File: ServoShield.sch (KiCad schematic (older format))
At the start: 54 parts, among them P1 M03, P10 M03, P11 M03, P12 M03, P13 M03, P14 M03, P15 M03, P16 M03, P2 M03, P3 M03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

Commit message: Completed v1.0
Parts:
- R9: value 14k -> 8K
- gave numbers to parts that had none: 1
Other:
- note added: "1.5A max output current\n"
- note added: "6V 1.5A Servo Power Supply\n"
- note added: "Default i2c\nAddress 0x40"
- note removed: "1A max output current\n"
- note removed: "6V 1A Servo Power Supply\n"

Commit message: Small tweaks
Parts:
- C1, C5: value 10uF -> 10uF 10V
- C2: value 68uF 25V -> 68uF 10V
- C3, C7: value 1uF -> 1uF 25V
- D1: value B540C -> B340 40V 3A

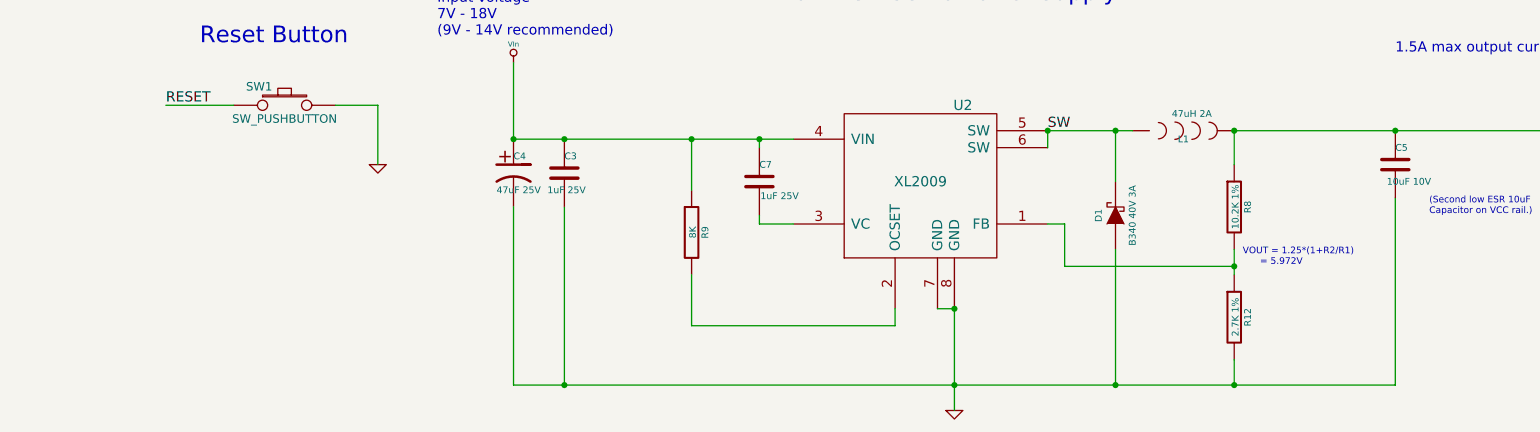
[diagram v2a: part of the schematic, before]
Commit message: V1.1: Add power LED, fix SSOP footprint for PCA9685
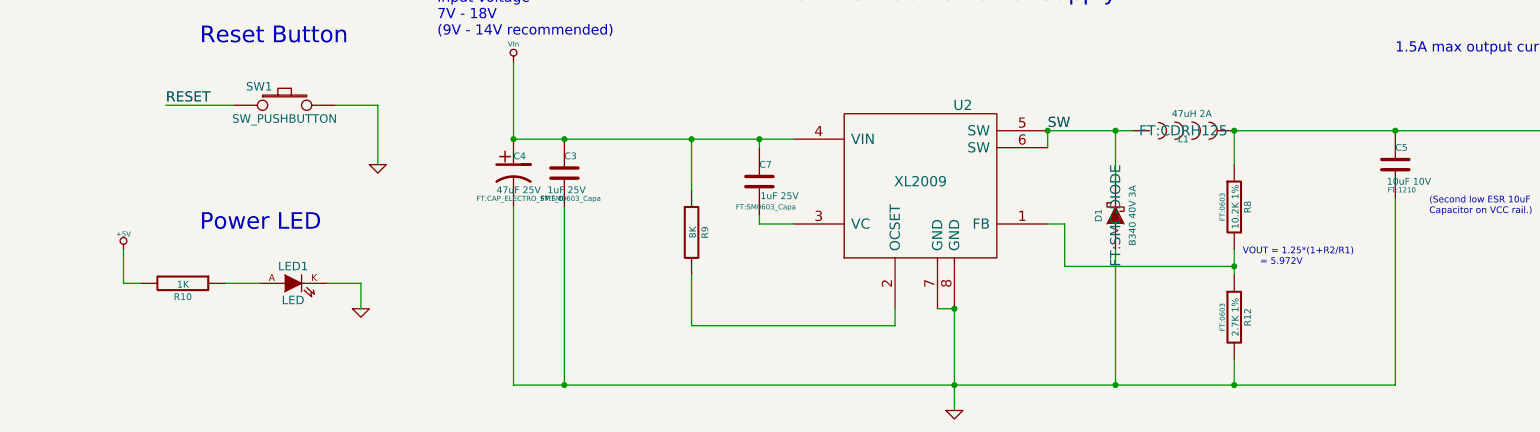
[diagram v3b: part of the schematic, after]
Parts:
- added LED1: LED, FT:LED-0603, symbol LED
- added R10: 1K, FT:0603, symbol R
- C1: footprint (none) -> FT:1210
- C2: footprint (none) -> FT:CAP_ELECTRO_SMT_D
- C3, C7: footprint ~ -> FT:SM0603_Capa
- C4: footprint ~ -> FT:CAP_ELECTRO_SMT_D
- C5: footprint ~ -> FT:1210
- C6: footprint (none) -> FT:SM0603_Capa
- D1: footprint ~ -> FT:SMC-DIODE
- JP1, JP4: footprint (none) -> FT:1X08
- JP2: footprint (none) -> FT:1X06
- JP3: footprint (none) -> FT:1X10
- JP5, P1, P10, P11, P12, P13, P14, P15, P16, P2, P3, P4, P5, P6, P7, P8, P9: footprint (none) -> FT:1X03
- L1: footprint ~ -> FT:CDRH125
- Q1, Q2: footprint (none) -> FT:SOT323_MOSFET
- R1, R2, R3, R4, R6, R7: footprint (none) -> FT:RES_CAY16
- R12, R8: footprint ~ -> FT:0603
- R5, R9: footprint (none) -> FT:0603
- SHIELD1: footprint (none) -> FT:ARDUINO_SHIELD
- SJ1, SJ2, SJ3, SJ4, SJ5, SJ6, SJ7, SJ8: footprint (none) -> FT:SJ_OPEN
- SW1: footprint (none) -> FT:TACTILE_SWITCH_SMD_2PIN_TINY
- U1: footprint (none) -> FT:SSOP28-4.4MM
- U2: footprint (none) -> FT:SO08
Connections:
- wire segments 255 -> 260
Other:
- note added: "Power LED"

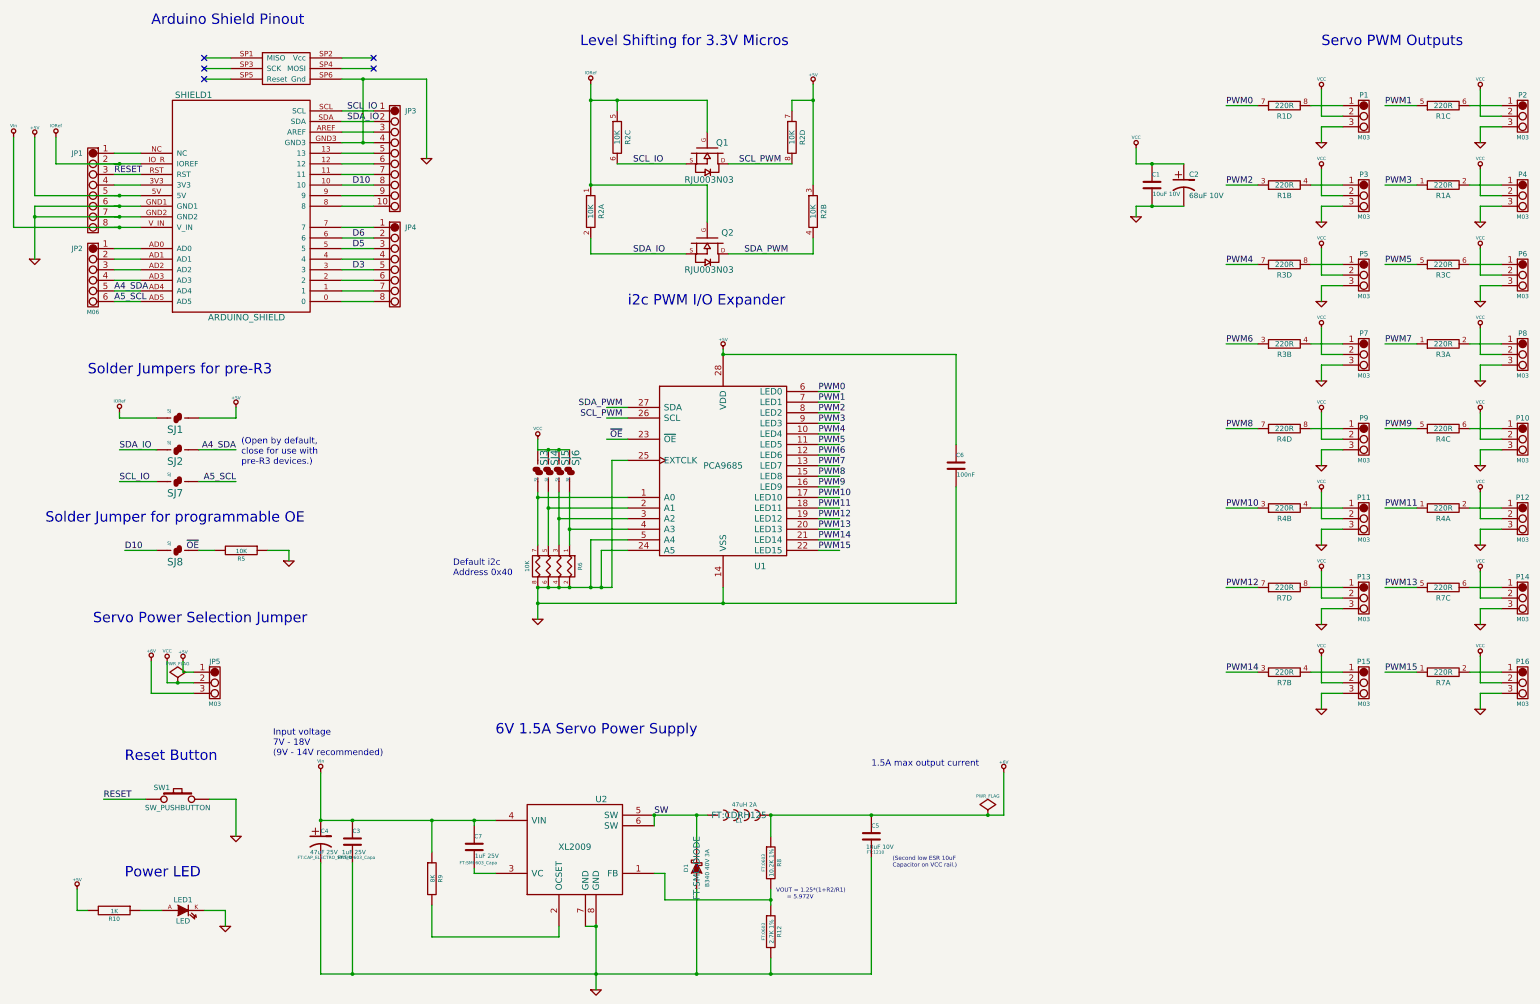
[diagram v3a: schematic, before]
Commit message: Small V1.1 silkscreen cleanup, new library revision
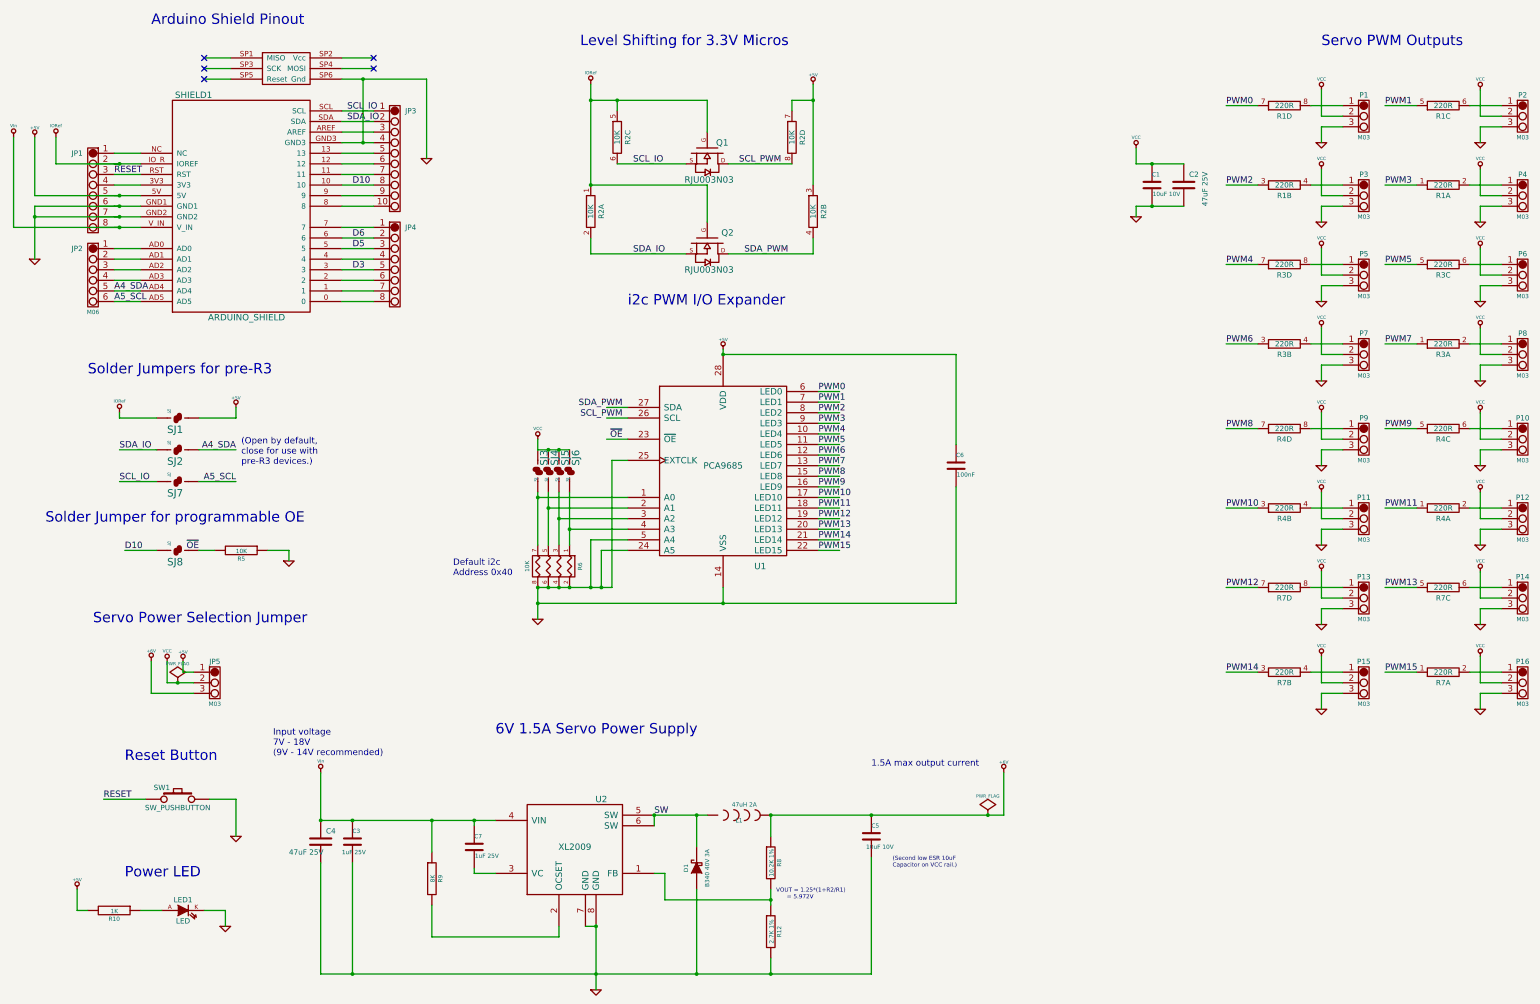
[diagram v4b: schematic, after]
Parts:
- removed C2: 68uF 10V, FT:CAP_ELECTRO_SMT_D, symbol CAP_POL
- removed C4: 47uF 25V, FT:CAP_ELECTRO_SMT_D, symbol CAP_POL
- added C2, C4: 47uF 25V, FT:CAP_ELECTRO_SMD_6.6mm, symbol CAP
- C3, C6, C7: footprint FT:SM0603_Capa -> FT:0603_CAP
- D1: footprint FT:SMC-DIODE -> FT:DIODE_SMC
- L1: footprint FT:CDRH125 -> FT:IND_CDRH125
- Q1, Q2: footprint FT:SOT323_MOSFET -> FT:SOT323_FET
- SW1: footprint FT:TACTILE_SWITCH_SMD_2PIN_TINY -> FT:SW_PUSHBUTTON_TINY_2PIN
- U1: footprint FT:SSOP28-4.4MM -> FT:SSOP28_4mm
- U2: footprint FT:SO08 -> FT:SO08_4mm
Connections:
- wire segments 260 -> 299
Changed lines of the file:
@@
 EESchema Schematic File Version 2
-LIBS:freetronics_kicad_sch_lib
+LIBS:freetronics_schematic
 LIBS:power
 LIBS:device
@@
 F 0 "U1" H 7900 4950 60  0000 C CNN
 F 1 "PCA9685" H 7550 5900 60  0000 C CNN
-F 2 "FT:SSOP28-4.4MM" H 7900 5850 60  0001 C CNN
+F 2 "FT:SSOP28_4mm" H 7900 5850 60  0001 C CNN
 F 3 "" H 7900 5850 60  0000 C CNN
 	1    7550 5850
@@
 F 0 "Q1" V 7300 3050 60  0000 R CNN
 F 1 "RJU003N03" V 7650 3100 60  0000 R CNN
-F 2 "FT:SOT323_MOSFET" H 7400 2850 60  0001 C CNN
+F 2 "FT:SOT323_FET" H 7400 2850 60  0001 C CNN
 F 3 "" H 7400 2850 60  0000 C CNN
 	1    7400 2850
@@
 F 0 "Q2" V 7300 3950 60  0000 R CNN
 F 1 "RJU003N03" V 7650 3950 60  0000 R CNN
-F 2 "FT:SOT323_MOSFET" H 7400 3700 60  0001 C CNN
+F 2 "FT:SOT323_FET" H 7400 3700 60  0001 C CNN
 F 3 "" H 7400 3700 60  0000 C CNN
 	1    7400 3700
@@
 F 0 "L1" H 7700 9050 40  0000 C CNN
 F 1 "47uH 2A" H 7750 9200 40  0000 C CNN
-F 2 "FT:CDRH125" H 7700 9100 60  0000 C CNN
+F 2 "FT:IND_CDRH125" H 7700 9100 60  0001 C CNN
 F 3 "~" H 7700 9100 60  0000 C CNN
 	1    7700 9100
@@
 F 0 "R8" V 8080 9550 40  0000 C CNN
 F 1 "10.2K 1%" V 8007 9551 40  0000 C CNN
-F 2 "FT:0603" V 7930 9550 30  0000 C CNN
+F 2 "FT:0603" V 7930 9550 30  0001 C CNN
 F 3 "~" H 8000 9550 30  0000 C CNN
 	1    8000 9550
@@
 F 0 "R12" V 8080 10200 40  0000 C CNN
 F 1 "2.7K 1%" V 8007 10201 40  0000 C CNN
-F 2 "FT:0603" V 7930 10200 30  0000 C CNN
+F 2 "FT:0603" V 7930 10200 30  0001 C CNN
 F 3 "~" H 8000 10200 30  0000 C CNN
 	1    8000 10200
@@
 F 0 "C5" H 8950 9400 40  0000 L CNN
 F 1 "10uF 10V" H 8900 9200 40  0000 L CNN
-F 2 "FT:1210" H 8988 9150 30  0000 C CNN
+F 2 "FT:1210" H 8988 9150 30  0001 C CNN
 F 3 "~" H 8950 9300 60  0000 C CNN
 	1    8950 9300
@@
 F 0 "C7" H 5200 9500 40  0000 L CNN
 F 1 "1uF 25V" H 5206 9315 40  0000 L CNN
-F 2 "FT:SM0603_Capa" H 5238 9250 30  0000 C CNN
+F 2 "FT:0603_CAP" H 5238 9250 30  0001 C CNN
 F 3 "~" H 5200 9400 60  0000 C CNN
 	1    5200 9400
@@
 Text Notes 8950 8650 0    60   ~ 0
 1.5A max output current\n
-$Comp
-L CAP_POL C4
-U 1 1 53EF71F2
-P 3750 9350
-F 0 "C4" H 3750 9450 40  0000 L CNN
-F 1 "47uF 25V" H 3650 9250 40  0000 L CNN
-F 2 "FT:CAP_ELECTRO_SMT_D" H 3788 9200 30  0000 C CNN
-F 3 "~" H 3750 9350 60  0000 C CNN
-	1    3750 9350
-	1    0    0    -1
-$EndComp
 Text Notes 9150 9600 0    39   ~ 0
 (Second low ESR 10uF\nCapacitor on VCC rail.)
@@
 F 0 "D1" H 7300 9700 40  0000 C CNN
 F 1 "B340 40V 3A" H 7300 9500 40  0000 C CNN
-F 2 "FT:SMC-DIODE" H 7300 9600 60  0000 C CNN
+F 2 "FT:DIODE_SMC" H 7300 9600 60  0001 C CNN
 F 3 "~" H 7300 9600 60  0000 C CNN
 	1    7300 9600
@@
 F 0 "SW1" H 2250 9060 50  0000 C CNN
 F 1 "SW_PUSHBUTTON" H 2400 8870 50  0000 C CNN
-F 2 "FT:TACTILE_SWITCH_SMD_2PIN_TINY" H 2400 8950 60  0001 C CNN
+F 2 "FT:SW_PUSHBUTTON_TINY_2PIN" H 2400 8950 60  0001 C CNN
 F 3 "" H 2400 8950 60  0000 C CNN
 	1    2400 8950
@@
 $EndComp
 $Comp
-L CAP_POL C2
-U 1 1 53ED3090
-P 11900 3150
-F 0 "C2" H 11950 3250 50  0000 L CNN
-F 1 "68uF 10V" H 11950 3050 50  0000 L CNN
-F 2 "FT:CAP_ELECTRO_SMT_D" H 11900 3150 60  0001 C CNN
-F 3 "" H 11900 3150 60  0000 C CNN
-	1    11900 3150
-	1    0    0    -1
-$EndComp
-$Comp
 L VIn #PWR054
 U 1 1 53ED1F31
@@
 F 0 "C3" H 4050 9450 40  0000 L CNN
 F 1 "1uF 25V" H 3950 9250 40  0000 L CNN
-F 2 "FT:SM0603_Capa" H 4088 9200 30  0000 C CNN
+F 2 "FT:0603_CAP" H 4088 9200 30  0001 C CNN
 F 3 "~" H 4050 9350 60  0000 C CNN
 	1    4050 9350
@@
 F 0 "U2" H 6400 9850 60  0000 C CNN
 F 1 "XL2009" H 6150 9400 60  0000 C CNN
-F 2 "FT:SO08" H 5950 8950 60  0001 C CNN
+F 2 "FT:SO08_4mm" H 5950 8950 60  0001 C CNN
 F 3 "" H 5950 8950 60  0000 C CNN
 	1    6150 9400
@@
 F 0 "C6" H 9750 5900 40  0000 L CNN
 F 1 "100nF" H 9756 5715 40  0000 L CNN
-F 2 "FT:SM0603_Capa" H 9788 5650 30  0001 C CNN
+F 2 "FT:0603_CAP" H 9788 5650 30  0001 C CNN
 F 3 "" H 9750 5800 60  0000 C CNN
 	1    9750 5800
@@
 	3950 1950 4250 1950
 Wire Wire Line
-	3950 2150 4750 2150
-Wire Wire Line
-	1800 3450 2050 3450
+	3950 2150 4150 2150
+Wire Wire Line
+	4150 2150 4750 2150
+Wire Wire Line
+	1800 3450 1850 3450
+Wire Wire Line
+	1850 3450 2050 3450
 Wire Wire Line
 	3950 4250 4250 4250
@@
 	3950 2850 4250 2850
 Wire Wire Line
-	3950 2750 4250 2750
+	3950 2750 4150 2750
+Wire Wire Line
+	4150 2750 4250 2750
 Wire Wire Line
 	3950 2650 4250 2650
@@
 	2050 3750 1800 3750
 Wire Wire Line
-	1800 3550 2050 3550
-Wire Wire Line
-	1800 3350 2050 3350
-Wire Wire Line
-	1800 3250 2050 3250
+	1800 3550 1850 3550
+Wire Wire Line
+	1850 3550 2050 3550
+Wire Wire Line
+	1800 3350 1850 3350
+Wire Wire Line
+	1850 3350 2050 3350
+Wire Wire Line
+	1800 3250 1850 3250
+Wire Wire Line
+	1850 3250 2050 3250
 Wire Wire Line
 	2050 3150 1800 3150
@@
 	2050 3050 1800 3050
 Wire Wire Line
-	1800 2950 2050 2950
+	1800 2950 1850 2950
+Wire Wire Line
+	1850 2950 2050 2950
 Wire Wire Line
 	2050 2850 1800 2850
 Wire Wire Line
-	8400 2200 8400 3150
+	8400 2200 8400 2350
+Wire Wire Line
+	8400 2350 8400 3150
 Connection ~ 8400 2350
 Wire Wire Line
@@
 	6550 2350 6550 2450
 Wire Wire Line
-	6300 2350 7400 2350
+	6300 2350 6550 2350
+Wire Wire Line
+	6550 2350 7400 2350
 Wire Wire Line
 	8400 3800 8400 3650
@@
 	11450 3350 11450 3450
 Wire Wire Line
-	11450 3350 11900 3350
+	11450 3350 11600 3350
+Wire Wire Line
+	11600 3350 11900 3350
 Connection ~ 11600 2950
 Wire Wire Line
 	11450 2950 11450 2800
 Wire Wire Line
-	11450 2950 11900 2950
+	11450 2950 11600 2950
+Wire Wire Line
+	11600 2950 11900 2950
 Wire Wire Line
 	3750 9150 3750 8700
@@
 Connection ~ 8000 9900
 Wire Wire Line
-	8000 9800 8000 9950
+	8000 9800 8000 9900
+Wire Wire Line
+	8000 9900 8000 9950
 Connection ~ 8000 10600
 Wire Wire Line
-	3750 9150 5400 9150
-Wire Wire Line
-	6900 9100 7400 9100
-Wire Wire Line
-	8000 9100 10200 9100
+	3750 9150 4050 9150
+Wire Wire Line
+	4050 9150 4800 9150
+Wire Wire Line
+	4800 9150 5200 9150
+Wire Wire Line
+	5200 9150 5400 9150
+Wire Wire Line
+	6900 9100 7300 9100
+Wire Wire Line
+	7300 9100 7400 9100
+Wire Wire Line
+	8000 9100 8950 9100
+Wire Wire Line
+	8950 9100 10050 9100
+Wire Wire Line
+	10050 9100 10200 9100
 Wire Wire Line
 	8000 10600 8000 10450
@@
 Connection ~ 5800 7100
 Wire Wire Line
-	5800 7100 9750 7100
+	5800 7100 7550 7100
+Wire Wire Line
+	7550 7100 9750 7100
 Wire Wire Line
 	7550 6950 7550 7100
 Wire Wire Line
-	5800 6950 6500 6950
+	5800 6950 5900 6950
+Wire Wire Line
+	5900 6950 6000 6950
+Wire Wire Line
+	6000 6950 6100 6950
+Wire Wire Line
+	6100 6950 6300 6950
+Wire Wire Line
+	6300 6950 6400 6950
+Wire Wire Line
+	6400 6950 6500 6950
 Connection ~ 6300 6950
 Wire Wire Line
@@
 	2150 7950 2550 7950
 Wire Wire Line
-	2300 7850 2550 7850
+	2300 7850 2400 7850
+Wire Wire Line
+	2400 7850 2550 7850
 Wire Wire Line
 	2450 7750 2450 7650
@@
 Connection ~ 6000 5650
 Wire Wire Line
-	5800 5650 6100 5650
+	5800 5650 5900 5650
+Wire Wire Line
+	5900 5650 6000 5650
+Wire Wire Line
+	6000 5650 6100 5650
 Wire Wire Line
 	6450 5550 6650 5550
@@
 	8650 5100 8450 5100
 Wire Wire Line
-	5800 6950 5800 7250
+	5800 6950 5800 7100
+Wire Wire Line
+	5800 7100 5800 7250
 Connection ~ 5800 6100
 Wire Wire Line
-	5800 6050 5800 6550
+	5800 6050 5800 6100
+Wire Wire Line
+	5800 6100 5800 6550
 Wire Wire Line
 	6650 6100 5800 6100
 Connection ~ 5900 6200
 Wire Wire Line
-	5900 6050 5900 6550
+	5900 6050 5900 6200
+Wire Wire Line
+	5900 6200 5900 6550
 Wire Wire Line
 	6650 6200 5900 6200
 Connection ~ 6000 6300
 Wire Wire Line
-	6000 6050 6000 6550
+	6000 6050 6000 6300
+Wire Wire Line
+	6000 6300 6000 6550
 Wire Wire Line
 	6650 6300 6000 6300
 Connection ~ 6100 6400
 Wire Wire Line
-	6100 6050 6100 6550
+	6100 6050 6100 6400
+Wire Wire Line
+	6100 6400 6100 6550
 Wire Wire Line
 	6650 6400 6100 6400
@@
 	1850 3350 1050 3350
 Wire Wire Line
-	1050 3350 1050 3850
+	1050 3350 1050 3450
+Wire Wire Line
+	1050 3450 1050 3850
 Wire Wire Line
 	1850 3450 1050 3450
@@
 	6250 10150 6350 10150
 Wire Wire Line
-	6350 10150 6350 10750
+	6350 10150 6350 10600
+Wire Wire Line
+	6350 10600 6350 10750
 Connection ~ 6350 10600
 Connection ~ 6350 10150
@@
 	7000 9900 8000 9900
 Wire Wire Line
-	3750 10600 8950 10600
+	3750 10600 4050 10600
+Wire Wire Line
+	4050 10600 6350 10600
+Wire Wire Line
+	6350 10600 7300 10600
+Wire Wire Line
+	7300 10600 8000 10600
+Wire Wire Line
+	8000 10600 8950 10600
 Wire Wire Line
 	7300 9400 7300 9100
@@
 	9750 7100 9750 6000
 Wire Wire Line
-	6300 2200 6300 3150
+	6300 2200 6300 2350
+Wire Wire Line
+	6300 2350 6300 3150
 $Comp
 L IORef #PWR056
@@
 Text Notes 1900 9700 0    98   ~ 0
 Power LED
+$Comp
+L CAP C4
+U 1 1 547D1A26
+P 3750 9350
+F 0 "C4" H 3800 9450 50  0000 L CNN
+F 1 "47uF 25V" H 3450 9250 50  0000 L CNN
+F 2 "FT:CAP_ELECTRO_SMD_6.6mm" H 3750 9350 60  0001 C CNN
+F 3 "" H 3750 9350 60  0000 C CNN
+	1    3750 9350
+	1    0    0    -1
+$EndComp
+$Comp
+L CAP C2
+U 1 1 547D31E3
+P 11900 3150
+F 0 "C2" H 11950 3250 50  0000 L CNN
+F 1 "47uF 25V" V 12100 2950 50  0000 L CNN
+F 2 "FT:CAP_ELECTRO_SMD_6.6mm" H 11900 3150 60  0001 C CNN
+F 3 "" H 11900 3150 60  0000 C CNN
+	1    11900 3150
+	1    0    0    -1
+$EndComp
 $EndSCHEMATC
